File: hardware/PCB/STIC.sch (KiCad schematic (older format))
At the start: 15 parts, among them J1 22-03-5035, J2 53047-0510, J3 53047-0310, U1 XIAO_BLE, U2 RM3100_Breakout, U3 OLED1_3_GND1

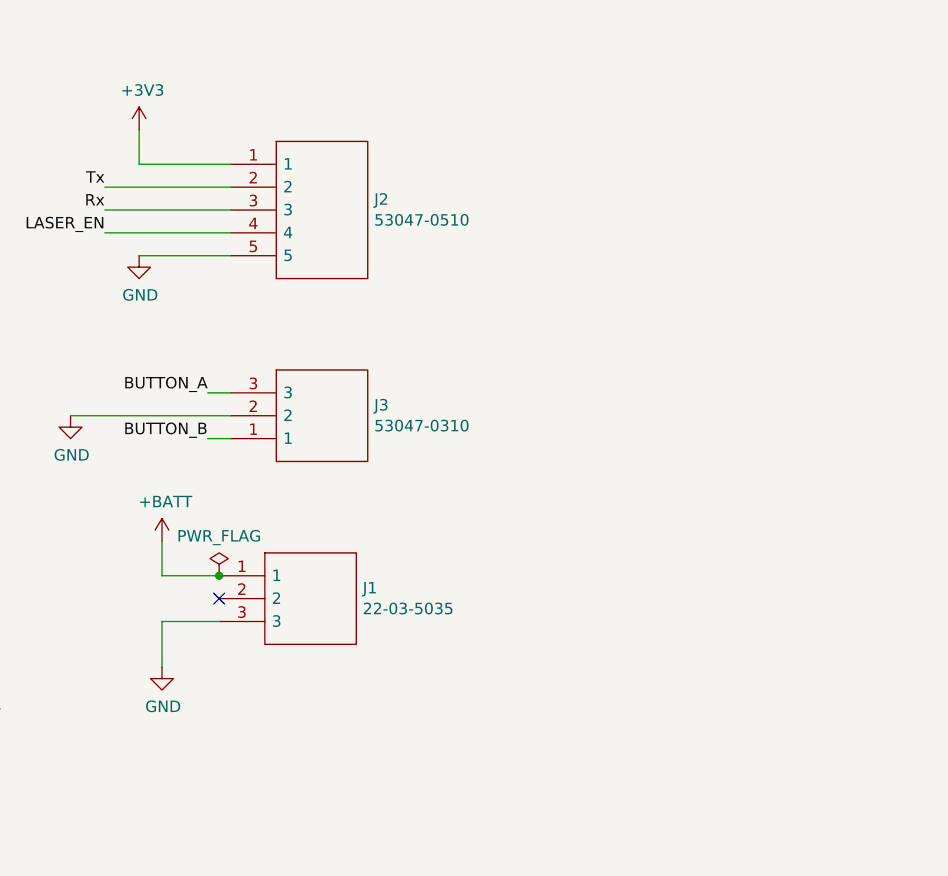
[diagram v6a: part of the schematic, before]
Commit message: Various PCB work
Add laser and battery to schematic (but not board, obvs)
Add second battery connector to allow JST-PH2 connectors
Add helpful silkscreen to board
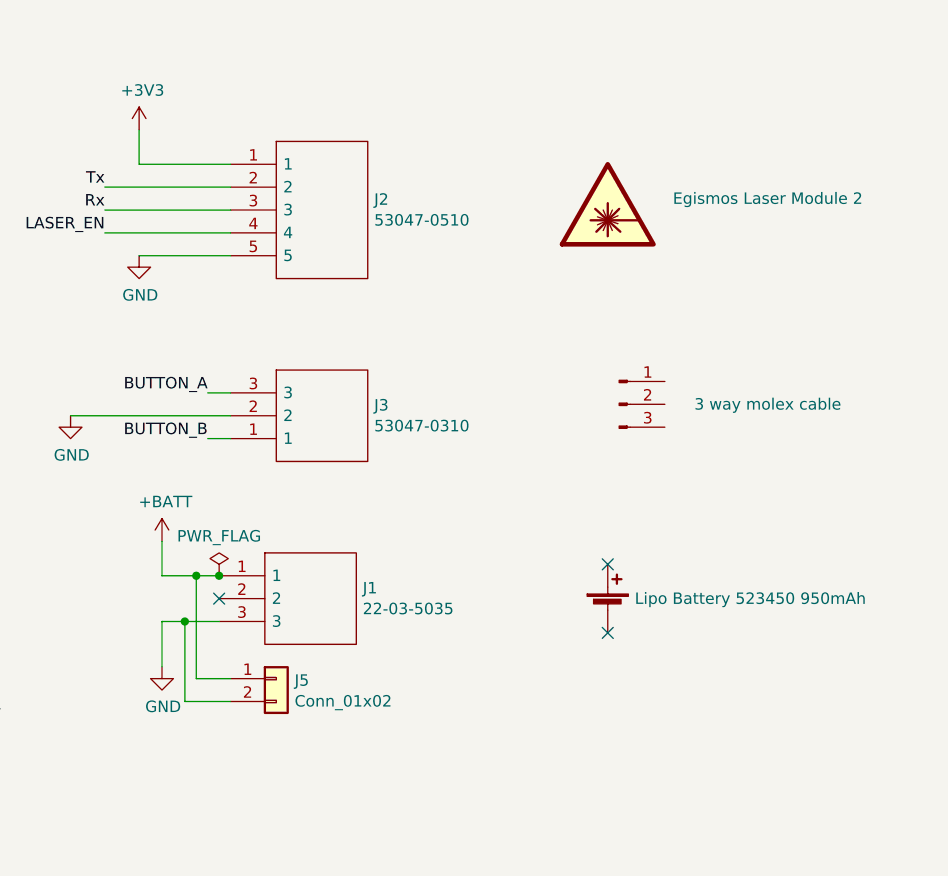
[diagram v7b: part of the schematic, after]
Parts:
- added BT1: Lipo Battery 523450 950mAh, symbol Device:Battery_Cell
- added J4: 3 way molex cable, symbol Connector:Conn_01x03_Male
- added J5: Conn_01x02, Connector_JST:JST_PH_B2B-PH-K_1x02_P2.00mm_Vertical, symbol Connector_Generic:Conn_01x02
- J1: Farnell Part Number (none) -> 9979620
- J2: Farnell Part Number (none) -> 9732861
- J3: Farnell Part Number (none) -> 9732853
- LS1: Farnell Part Number (none) -> 2433031; Manufacturer_Part_Number AST1240MLTRQ -> AST1240MLTRQ or MCABT-458-RC
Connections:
- net +BATT: now also J5.1 (Pin_1)
- net GND: now also J5.2 (Pin_2)
- no-connect marks 7 -> 9
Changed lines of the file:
@@
 F 2 "KiCad_imports:SPKR_AST1240MLTRQ" H 2100 6300 50  0001 C CNN
 F 3 "~" H 2090 6450 50  0001 C CNN
-F 4 "AST1240MLTRQ" H 2100 6500 50  0001 C CNN "Manufacturer_Part_Number"
+F 4 "AST1240MLTRQ or MCABT-458-RC " H 2100 6500 50  0001 C CNN "Manufacturer_Part_Number"
+F 5 "2433031" H 2100 6500 50  0001 C CNN "Farnell Part Number"
 	1    2100 6500
 	-1   0    0    1
@@
 F 9 "22-03-5035" H 8350 4050 50  0001 L CNN "Manufacturer_Part_Number"
 F 10 "70248167" H 8350 3950 50  0001 L CNN "Allied_Number"
+F 11 "9979620" H 7700 4650 50  0001 C CNN "Farnell Part Number"
 	1    7700 4650
 	1    0    0    -1
@@
 NoConn ~ 7700 4750
 Wire Wire Line
-	7700 4650 7450 4650
+	7700 4650 7600 4650
 Wire Wire Line
 	7450 4650 7450 4500
 Wire Wire Line
-	7700 4850 7450 4850
+	7700 4850 7550 4850
 Wire Wire Line
 	7450 4850 7450 5050
@@
 F 9 "53047-0510" H 8400 2250 50  0001 L CNN "Manufacturer_Part_Number"
 F 10 "70266929" H 8400 2150 50  0001 L CNN "Allied_Number"
+F 11 "9732861" H 7750 2850 50  0001 C CNN "Farnell Part Number"
 	1    7750 2850
 	1    0    0    -1
@@
 F 9 "53047-0310" H 8400 3250 50  0001 L CNN "Manufacturer_Part_Number"
 F 10 "70266925" H 8400 3150 50  0001 L CNN "Allied_Number"
+F 11 "9732853" H 7750 3850 50  0001 C CNN "Farnell Part Number"
 	1    7750 3850
 	1    0    0    -1
@@
 	3000 3750 2700 3750
 Connection ~ 2700 3750
+$Comp
+L Graphic:SYM_LASER_Large #SYM1
+U 1 1 65AA20FC
+P 9400 3000
+F 0 "#SYM1" H 9400 3200 50  0001 C CNN
+F 1 "Egismos Laser Module 2" H 10100 3000 50  0000 C CNN
+F 2 "" H 9390 2825 50  0001 C CNN
+F 3 "~" H 9430 2800 50  0001 C CNN
+	1    9400 3000
+	1    0    0    -1
+$EndComp
+$Comp
+L Device:Battery_Cell BT1
+U 1 1 65AA960B
+P 9400 4800
+F 0 "BT1" H 9518 4896 50  0001 L CNN
+F 1 "Lipo Battery 523450 950mAh" H 9518 4850 50  0000 L CNN
+F 2 "" V 9400 4860 50  0001 C CNN
+F 3 "https://cpc.farnell.com/unbranded/lp-523450-is-3/battery-lithium-pol-3-7v-950-mah/dp/BT06802" V 9400 4860 50  0001 C CNN
+F 4 "2077888 " H 9400 4800 50  0001 C CNN "Farnell Part Number"
+F 5 "LP-523450-IS-3" H 9400 4800 50  0001 C CNN "Manufacturer_Part_Number"
+	1    9400 4800
+	1    0    0    -1
+$EndComp
+NoConn ~ 9400 4600
+NoConn ~ 9400 4900
+$Comp
+L Connector:Conn_01x03_Male J4
+U 1 1 65ABAE89
+P 9450 3900
+F 0 "J4" H 9558 4181 50  0001 C CNN
+F 1 "3 way molex cable" H 10100 3900 50  0000 C CNN
+F 2 "" H 9450 3900 50  0001 C CNN
+F 3 "~" H 9450 3900 50  0001 C CNN
+F 4 "2913932 " H 9450 3900 50  0001 C CNN "Farnell Part Number"
+F 5 "15134-0301" H 9450 3900 50  0001 C CNN "Manufacturer_Part_Number"
+	1    9450 3900
+	1    0    0    -1
+$EndComp
+Wire Wire Line
+	7750 5200 7550 5200
+Wire Wire Line
+	7550 5200 7550 4850
+Connection ~ 7550 4850
+Wire Wire Line
+	7550 4850 7450 4850
+Wire Wire Line
+	7600 4650 7600 5100
+Wire Wire Line
+	7600 5100 7750 5100
+Connection ~ 7600 4650
+Wire Wire Line
+	7600 4650 7450 4650
+$Comp
+L Connector_Generic:Conn_01x02 J5
+U 1 1 65AC583E
+P 7950 5100
+F 0 "J5" H 8030 5092 50  0000 L CNN
+F 1 "Conn_01x02" H 8030 5001 50  0000 L CNN
+F 2 "Connector_JST:JST_PH_B2B-PH-K_1x02_P2.00mm_Vertical" H 7950 5100 50  0001 C CNN
+F 3 "~" H 7950 5100 50  0001 C CNN
+	1    7950 5100
+	1    0    0    -1
+$EndComp
 $EndSCHEMATC

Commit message: Add farnell part number
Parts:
- J5: Farnell Part Number (none) -> 9491856; Manufacturer_Part_Number (none) -> B2B-PH-K-S(LF)(SN)
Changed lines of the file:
@@
 F 2 "Connector_JST:JST_PH_B2B-PH-K_1x02_P2.00mm_Vertical" H 7950 5100 50  0001 C CNN
 F 3 "~" H 7950 5100 50  0001 C CNN
+F 4 "9491856 " H 7950 5100 50  0001 C CNN "Farnell Part Number"
+F 5 "B2B-PH-K-S(LF)(SN) " H 7950 5100 50  0001 C CNN "Manufacturer_Part_Number"
 	1    7950 5100
 	1    0    0    -1
